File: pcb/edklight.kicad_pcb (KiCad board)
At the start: 2 copper layers, 24 parts, among them J1 MotorIn, J2 ToLcd, J3 RearLight, J4 Fr Light, J5 2 But Ctrl, Q1 ZXMP4A16G, Q2 BSP89, Q3 BSP89, Q4 ZXMP4A16G, Q5 BSP89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

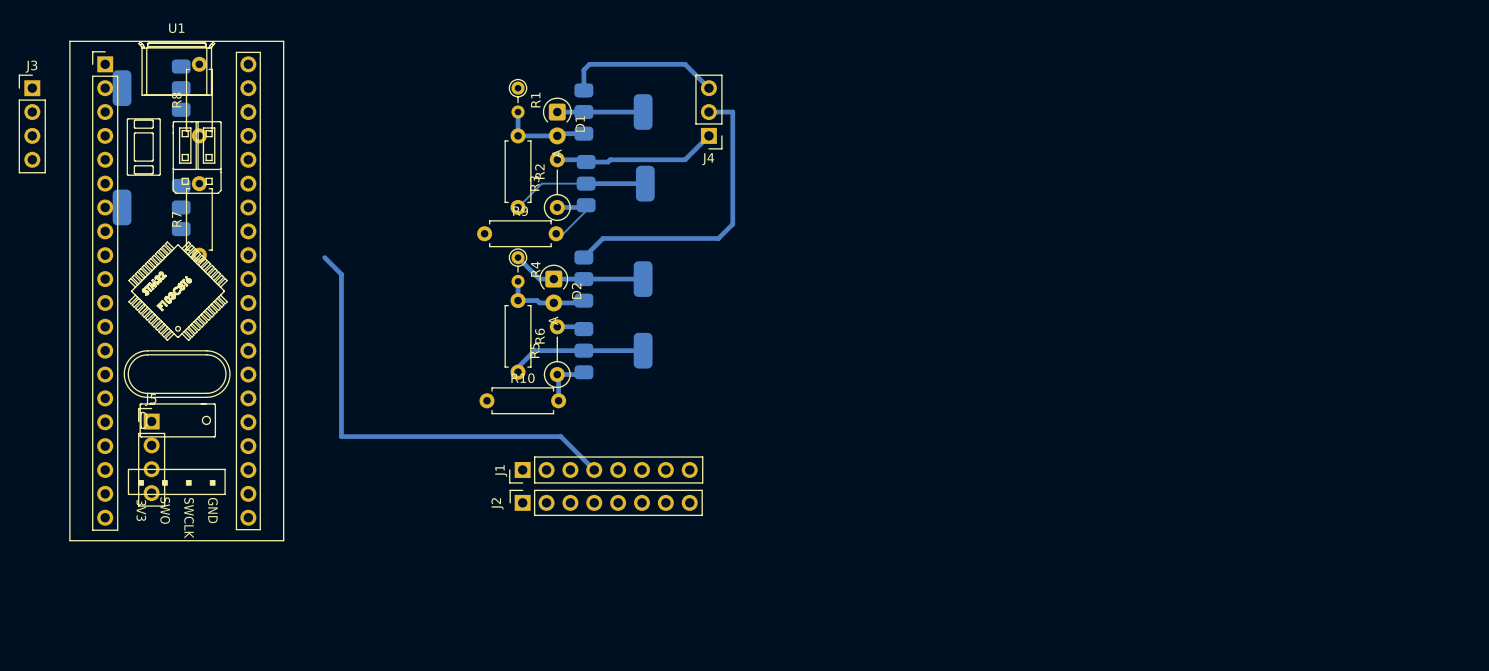
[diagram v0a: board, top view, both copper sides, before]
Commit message: note mcu brd, sch/ lib with BlackPill and Mini F103
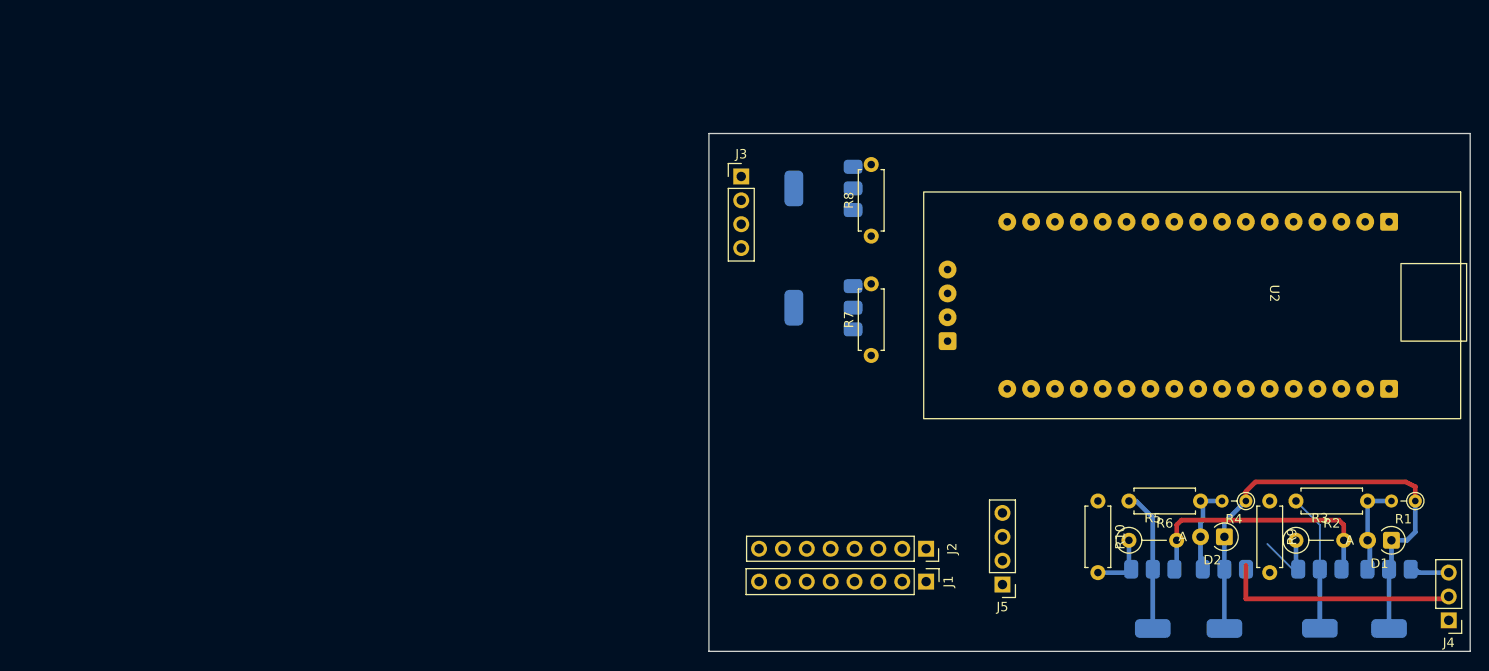
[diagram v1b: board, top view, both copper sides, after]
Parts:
- removed U1: YAAJ_WeAct_BlackPill_Part_Like, Footprints:YAAJ_BluePill_1
- added U2: ~, bp103_swd:bp103_swd, F.Cu at (156.2, 73.9)
- moved R1 105.1 mm to (174.2, 94.7), turned to 180 degrees
- moved D1 99.8 mm to (171.7, 98.9), turned to 180 degrees
- moved R2 98.4 mm to (169.2, 94.7), turned to 180 degrees
- moved Q1 97.5 mm to (171.4, 105.2), turned to -90 degrees
- moved J4 94.1 mm to (177.8, 107.4)
- moved J5 92.2 mm to (130.3, 103.6), turned to 180 degrees
- moved R9 88.3 mm to (158.8, 94.7), turned to -90 degrees
- moved Q3 87.0 mm to (164.1, 105.1), turned to -90 degrees
- moved R3 86.2 mm to (161.5, 98.9), turned to 0 degrees
- moved R4 81.7 mm to (156.2, 94.7), turned to 180 degrees
- moved D2 76.5 mm to (153.9, 98.6), turned to 180 degrees
- moved J3 76.0 mm to (102.5, 60.2)
- moved R6 75.7 mm to (151.4, 94.7), turned to 180 degrees
- moved Q4 73.4 mm to (153.9, 105.2), turned to -90 degrees
- moved Q5 72.3 mm to (111.3, 61.5)
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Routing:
- net RX: track 48.2 -> 0.00 mm
- net VDD: track 23.4 -> 51.3 mm
- net FLigh: track 16.8 -> 5.06 mm
- net GND: track 20.3 -> 27.8 mm
- net Horn: track 31.8 -> 25.3 mm
- net Net-(Q2-G): track 5.78 -> 7.01 mm
- net Net-(D2-A): track 10.1 -> 10.7 mm
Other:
- board outline added: 81 x 55.1 mm

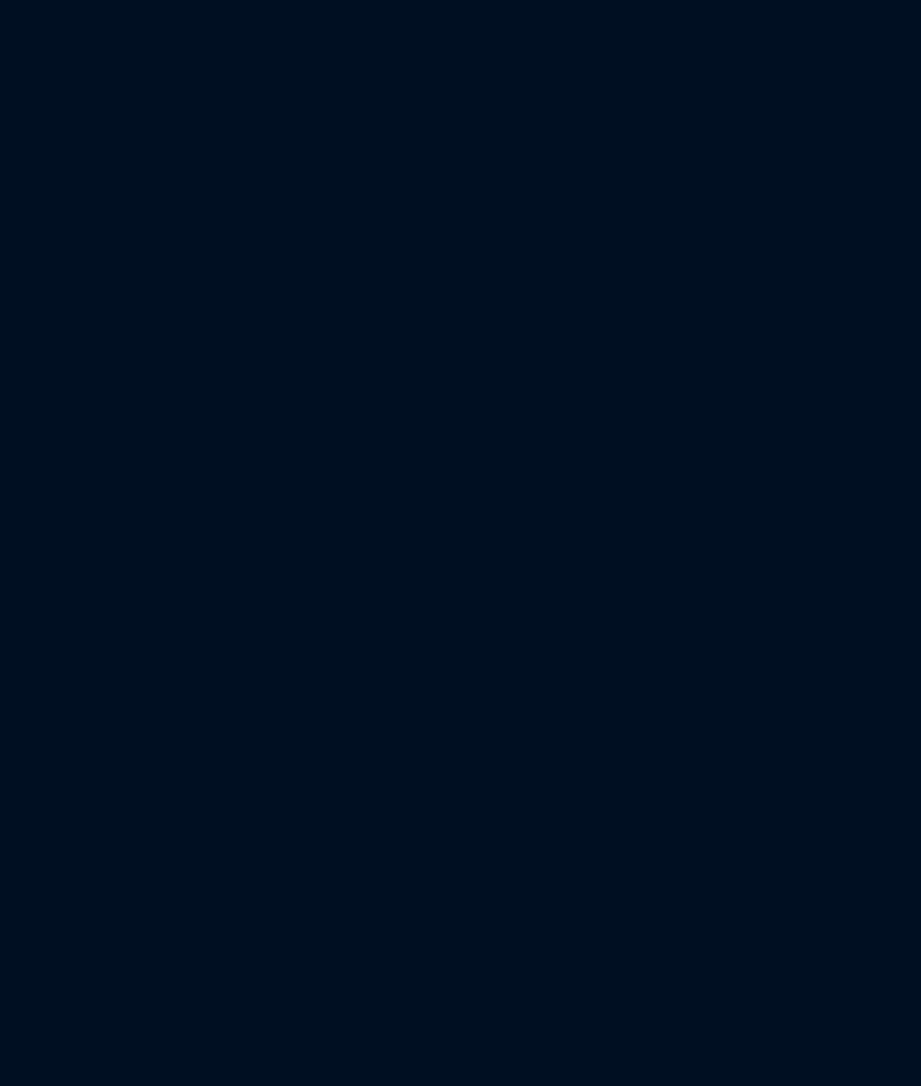
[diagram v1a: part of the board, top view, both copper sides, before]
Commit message: fix pins in mini103 and bp103
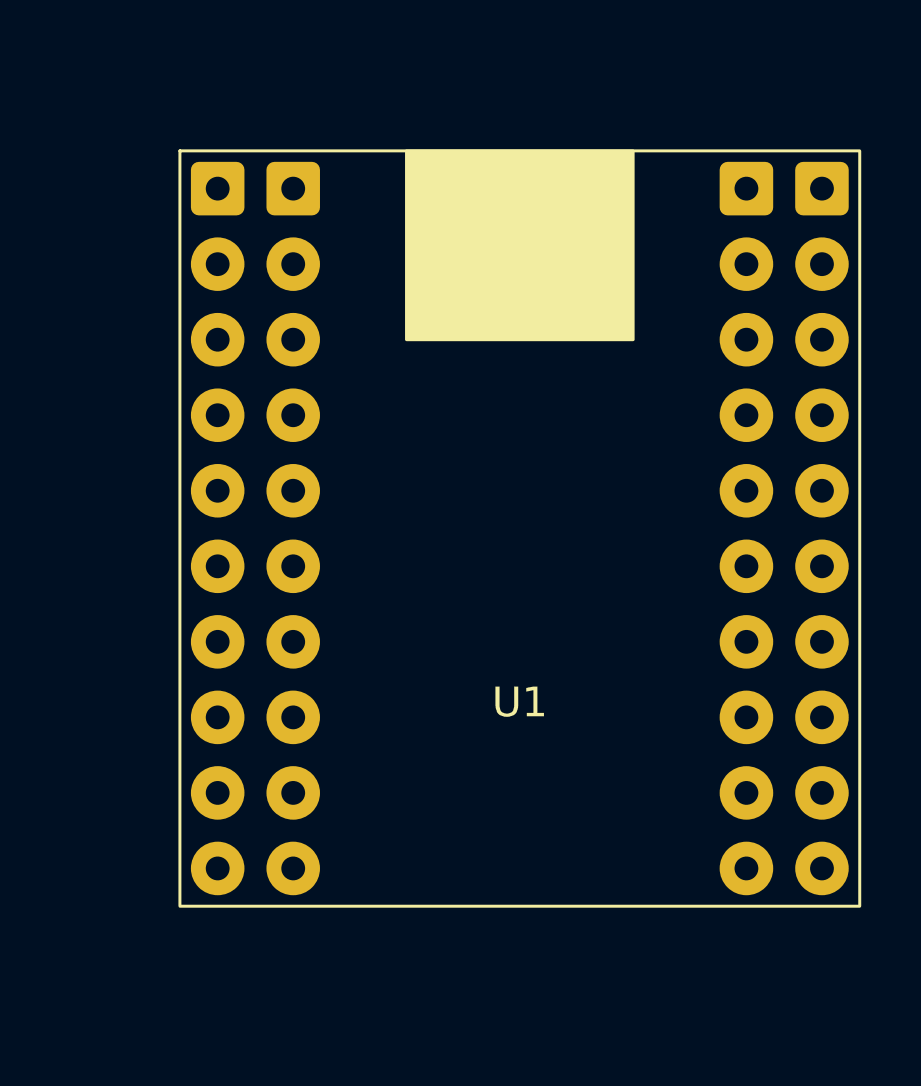
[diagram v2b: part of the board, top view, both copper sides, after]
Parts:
- added U1: ~, bp103_swd:MiniF103, F.Cu at (205.5, 70.1)

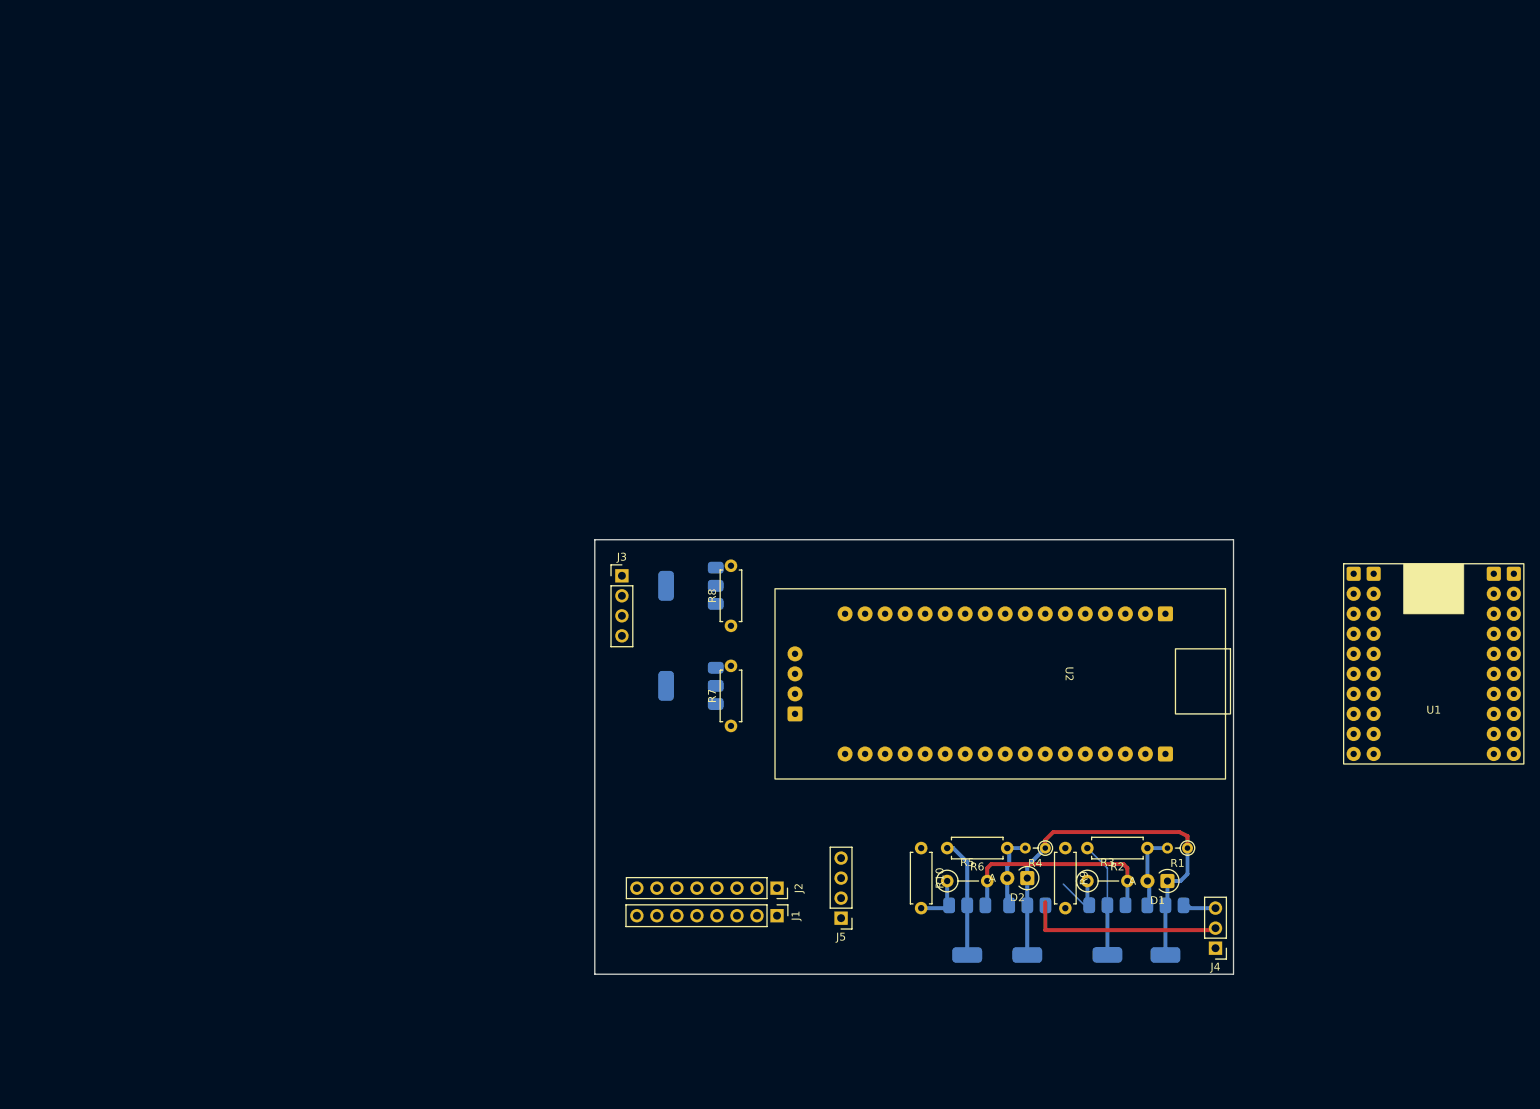
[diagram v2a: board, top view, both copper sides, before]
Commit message: pcb swicth to mini f103 updtae higo ,single pad for wire conection
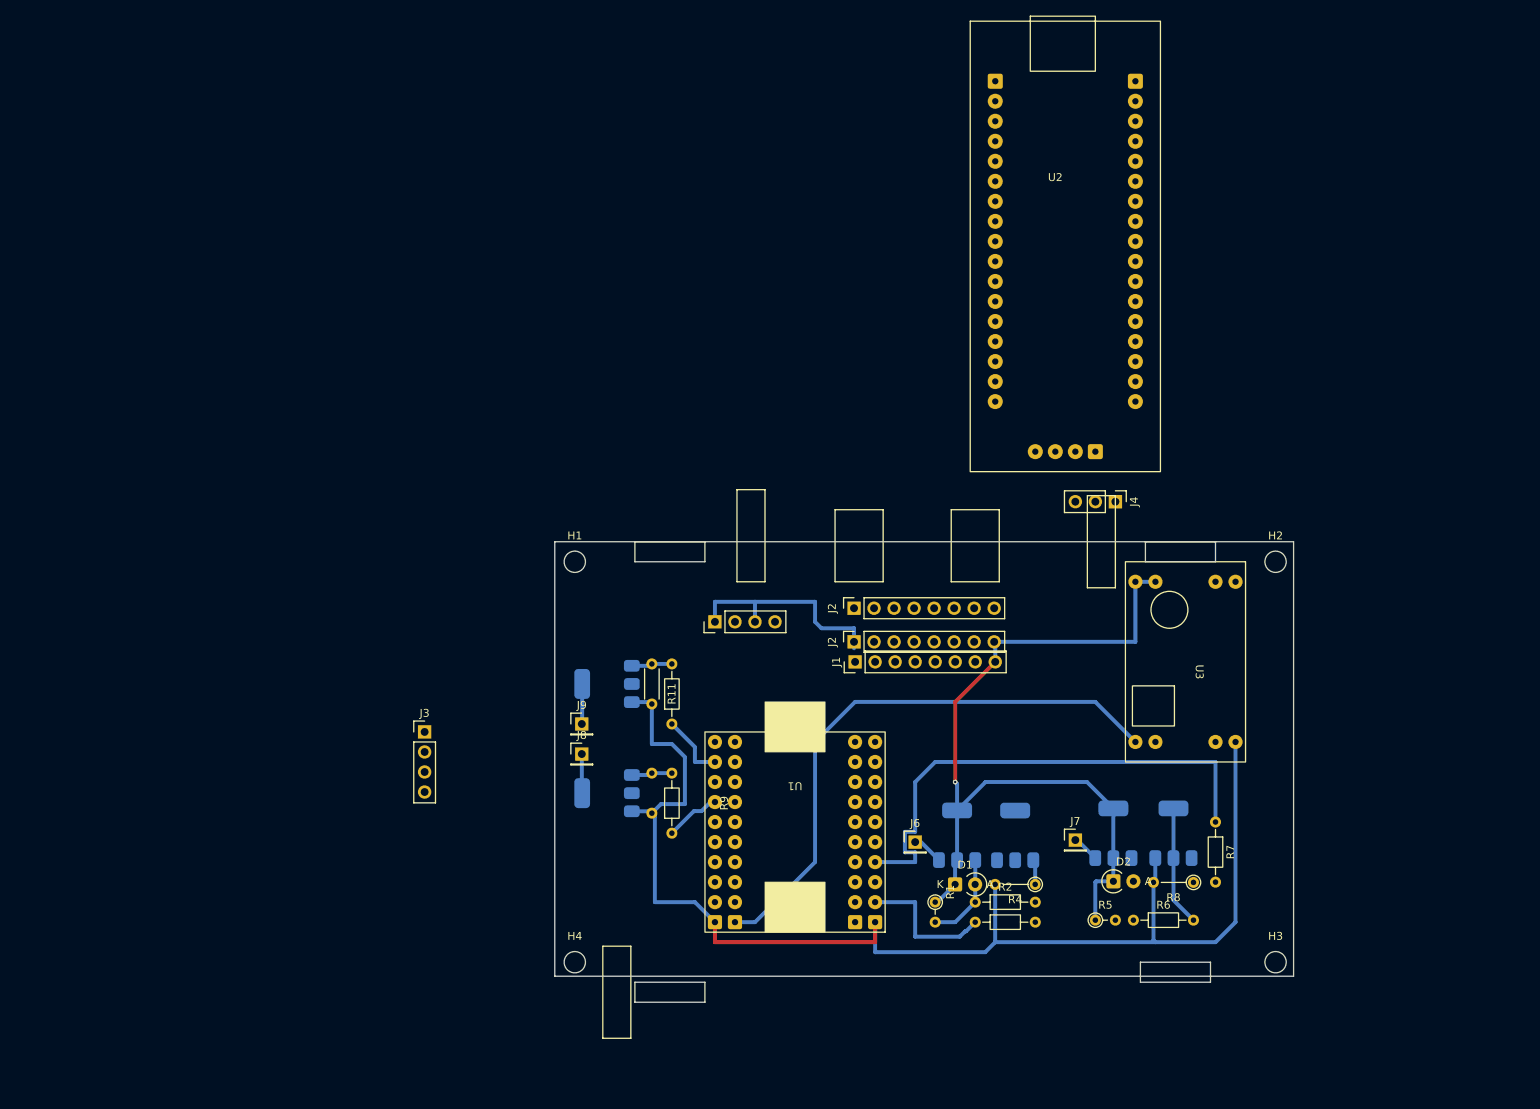
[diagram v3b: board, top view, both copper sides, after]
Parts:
- added H1: MountingHole, MountingHole:MountingHole_2.7mm_M2.5_DIN965, F.Cu at (96.5, 58.4)
- added H2: MountingHole, MountingHole:MountingHole_2.7mm_M2.5_DIN965, F.Cu at (185.4, 58.4)
- added H3: MountingHole, MountingHole:MountingHole_2.7mm_M2.5_DIN965, F.Cu at (185.4, 109.2)
- added H4: MountingHole, MountingHole:MountingHole_2.7mm_M2.5_DIN965, F.Cu at (96.5, 109.2)
- added J2: ToLcd, Connector_PinSocket_2.54mm:PinSocket_1x08_P2.54mm_Vertical, F.Cu at (131.9, 64.3)
- added J6: Conn_01x01_Pin, Connector_PinHeader_2.54mm:PinHeader_1x01_P2.54mm_Vertical, F.Cu at (139.7, 94.0)
- added J7: Conn_01x01_Pin, Connector_PinHeader_2.54mm:PinHeader_1x01_P2.54mm_Vertical, F.Cu at (160.0, 93.7)
- added J8: Conn_01x01_Pin, Connector_PinHeader_2.54mm:PinHeader_1x01_P2.54mm_Vertical, F.Cu at (97.4, 82.8)
- added J9: Conn_01x01_Pin, Connector_PinHeader_2.54mm:PinHeader_1x01_P2.54mm_Vertical, F.Cu at (97.4, 79.0)
- added R10: 10k, Resistor_THT:R_Axial_DIN0204_L3.6mm_D1.6mm_P5.08mm_Horizontal, B.Cu at (106.3, 85.2)
- added R12: 10k, Resistor_THT:R_Axial_DIN0204_L3.6mm_D1.6mm_P5.08mm_Horizontal, F.Cu at (106.3, 71.4)
- added U3: ~, bp103_swd:dce003, F.Cu at (175.3, 72.4)
- D1: footprint Diode_THT:D_A-405_P2.54mm_Vertical_AnodeUp -> Diode_THT:D_A-405_P2.54mm_Vertical_KathodeUp
- R11: renamed from R8; footprint Resistor_THT:R_Axial_DIN0207_L6.3mm_D2.5mm_P7.62mm_Horizontal -> Resistor_THT:R_Axial_DIN0204_L3.6mm_D1.6mm_P7.62mm_Horizontal
- R2, R6: footprint Resistor_THT:R_Axial_DIN0207_L6.3mm_D2.5mm_P7.62mm_Horizontal -> Resistor_THT:R_Axial_DIN0204_L3.6mm_D1.6mm_P7.62mm_Horizontal
- R3: renamed from R9; footprint Resistor_THT:R_Axial_DIN0207_L6.3mm_D2.5mm_P7.62mm_Horizontal -> Resistor_THT:R_Axial_DIN0204_L3.6mm_D1.6mm_P7.62mm_Horizontal
- R4: renamed from R3; value R_US -> 10K; footprint Resistor_THT:R_Axial_DIN0207_L6.3mm_D2.5mm_P5.08mm_Vertical -> Resistor_THT:R_Axial_DIN0204_L3.6mm_D1.6mm_P5.08mm_Vertical
- R7: renamed from R10; footprint Resistor_THT:R_Axial_DIN0207_L6.3mm_D2.5mm_P7.62mm_Horizontal -> Resistor_THT:R_Axial_DIN0204_L3.6mm_D1.6mm_P7.62mm_Horizontal
- R8: renamed from R5; value R_US -> 10k; footprint Resistor_THT:R_Axial_DIN0207_L6.3mm_D2.5mm_P5.08mm_Vertical -> Resistor_THT:R_Axial_DIN0204_L3.6mm_D1.6mm_P5.08mm_Vertical
- R9: renamed from R7; footprint Resistor_THT:R_Axial_DIN0207_L6.3mm_D2.5mm_P7.62mm_Horizontal -> Resistor_THT:R_Axial_DIN0204_L3.6mm_D1.6mm_P7.62mm_Horizontal
- moved U1 84.5 mm to (124.5, 94.0), turned to 180 degrees
- moved U2 61.3 mm to (158.8, 12.7), turned to 0 degrees
- moved J4 58.0 mm to (165.1, 50.8), turned to -90 degrees
- moved J5 40.9 mm to (114.3, 66.0), turned to 90 degrees
- moved R7 37.5 mm to (177.8, 91.4)
- moved J1 33.7 mm to (132.1, 71.1), turned to 90 degrees
- moved J2 32.7 mm to (131.9, 68.6), turned to 90 degrees
- moved R1 32.7 mm to (142.2, 101.6), turned to -90 degrees
- moved J3 31.9 mm to (77.5, 80.0)
- moved R8 31.2 mm to (175.0, 99.1), turned to 180 degrees
- moved Q1 29.0 mm to (145.0, 93.1), turned to 90 degrees
- moved Q2 28.9 mm to (172.5, 92.9), turned to 90 degrees
- moved D1 26.9 mm to (144.8, 99.3), turned to 0 degrees
- moved R2 22.9 mm to (147.3, 101.6), turned to 0 degrees
- moved R6 18.4 mm to (167.4, 103.9), turned to 0 degrees
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- renumbered R4 to R5
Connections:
- net /Red Vin renamed Net-(J1-Pin_3)
- net Net-(J1-Pin_7) renamed /Ora VIn
- J1 pad 2: VDD -> /blu throt
- J1 pad 5: +5VD -> BrakeIn
- J1 pad 6: BrakeIn -> /Green TX
- J1 pad 8: /Brown TX -> VDD
- J2 pad 2: VDD -> /blu throt
- J2 pad 5: +5VD -> BrakeIn
- J2 pad 6: BrakeIn -> /Green TX
- J2 pad 8: /Brown TX -> VDD
- J4 pad 1: GND -> unconnected-(J4-Pin_1-Pad1)
- J4 pad 2: Horn -> unconnected-(J4-Pin_2-Pad2)
- J4 pad 3: FLigh -> unconnected-(J4-Pin_3-Pad3)
- U1 pad 1: unconnected-(U1-GND-Pad1) -> GND
- U1 pad 11: unconnected-(U1-5V-Pad11) -> +5VD
- U1 pad 21: unconnected-(U1-GND-Pad21) -> GND
- U1 pad 22: unconnected-(U1-B14-Pad22) -> FLighOn
- U1 pad 24: unconnected-(U1-B10-Pad24) -> HornOn
- U1 pad 29: unconnected-(U1-A3-Pad29) -> RX
- U1 pad 30: unconnected-(U1-A1-Pad30) -> LighBut
- U1 pad 33: (no net) -> unconnected-(U1-B13-Pad33)
- U1 pad 39: unconnected-(U1-A2-Pad39) -> HornBut
- U1 pad 40: unconnected-(U1-A0-Pad40) -> BrakeIn
- U1 pad 7: unconnected-(U1-B5-Pad7) -> RBrakeOn
- U1 pad 9: unconnected-(U1-B8-Pad9) -> RLighOn
- U2 pad 11: RX -> unconnected-(U2-A10-Pad11)
- U2 pad 13: FLighOn -> unconnected-(U2-A8-Pad13)
- U2 pad 18: GND -> unconnected-(U2-GND-Pad18)
- U2 pad 23: BrakeIn -> unconnected-(U2-A0-Pad23)
- U2 pad 24: LighBut -> unconnected-(U2-A1-Pad24)
- U2 pad 25: HornBut -> unconnected-(U2-A2-Pad25)
- U2 pad 29: RBrakeOn -> unconnected-(U2-A7-Pad29)
- U2 pad 30: RLighOn -> unconnected-(U2-A6-Pad30)
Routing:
- net GND: track 27.8 -> 191.7 mm
- net +5VD: track 0.00 -> 73.4 mm
- net HornOn: track 0.00 -> 64.6 mm
- net VDD: track 51.3 -> 104.1 mm, vias 0 -> 2
- net Horn: track 25.3 -> 3.47 mm
- net FLighOn: track 0.00 -> 17.8 mm
- net Net-(Q3-D): track 14.6 -> 0.02 mm
- net Net-(D2-A): track 10.7 -> 0.00 mm
- net RLighOn: track 0.00 -> 8.57 mm
- net RBrakeOn: track 0.00 -> 7.10 mm
- net Net-(Q2-G): track 7.01 -> 0.00 mm
- net Net-(Q6-G): track 0.00 -> 5.18 mm
- net Net-(Q5-G): track 0.00 -> 5.18 mm
- net RLigh: track 0.00 -> 5.10 mm
- net RBrake: track 0.00 -> 4.98 mm
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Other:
- board size 81 x 55.1 mm -> 93.7 x 58.4 mm
